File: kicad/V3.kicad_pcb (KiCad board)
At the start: 2 copper layers, 175.6 x 118.3 mm, 62 parts, among them U2 CH9329, U3 USB_C_C393939

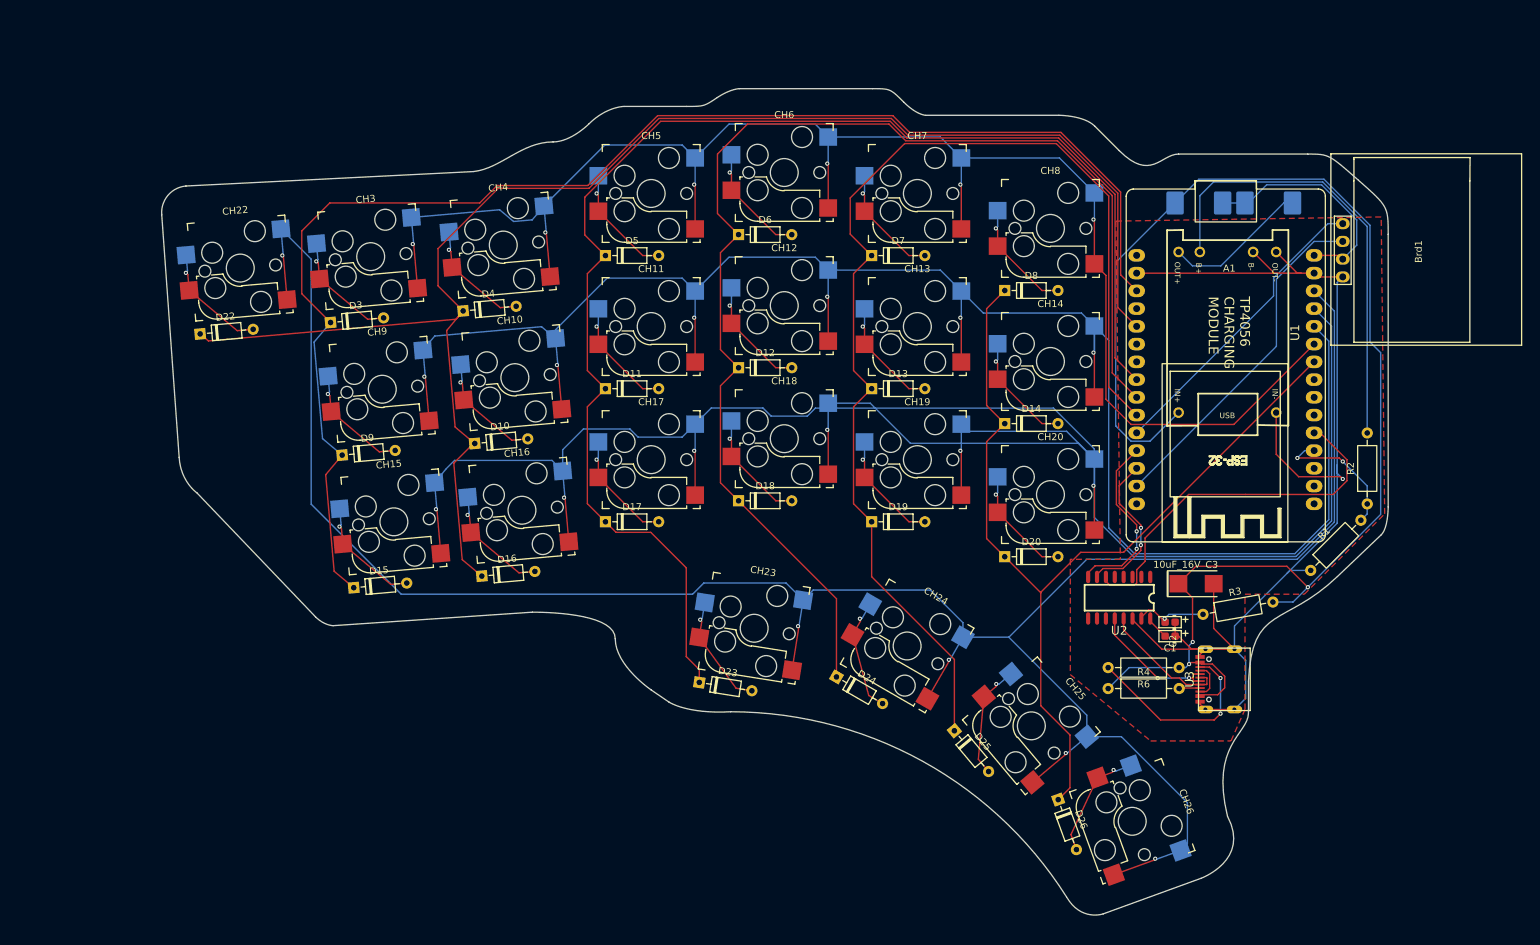
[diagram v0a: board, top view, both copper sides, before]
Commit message: switches change
switches no longer use heirarchical schematic
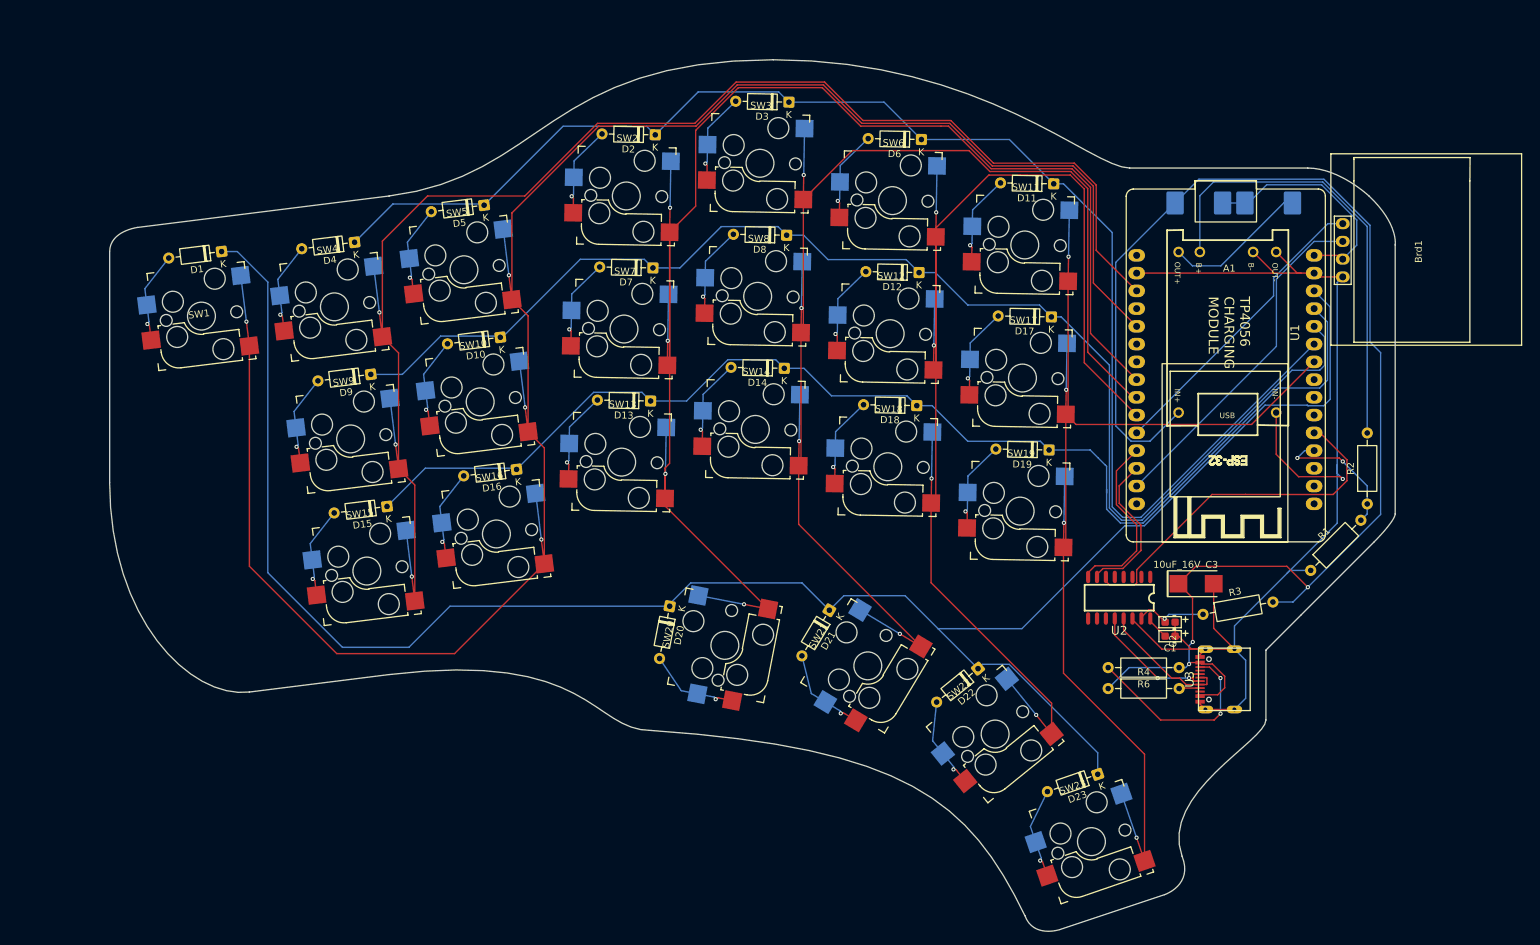
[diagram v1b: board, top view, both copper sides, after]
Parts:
- removed CH10, CH11, CH12, CH13, CH14, CH15, CH16, CH17, CH18, CH19, CH20, CH22, CH23, CH24, CH25, CH26, CH3, CH4, CH5, CH6, CH7, CH8, CH9: KS33_SW_HS, Library:Kailh_socket_MX_reversible
- removed D24, D25, D26: 1N4148, Diode_THT:D_DO-35_SOD27_P7.62mm_Horizontal
- added D1: 1N4148, Diode_THT:D_DO-35_SOD27_P7.62mm_Horizontal, F.Cu at (66.5, 64.0)
- added D2: 1N4148, Diode_THT:D_DO-35_SOD27_P7.62mm_Horizontal, F.Cu at (128.6, 47.2)
- added D21: 1N4148, Diode_THT:D_DO-35_SOD27_P7.62mm_Horizontal, F.Cu at (153.5, 115.3)
- added SW1: KS33_SW_HS, keyswitches:Kailh_socket_MX_reversible, F.Cu at (63.6, 73.2)
- added SW10: KS33_SW_HS, keyswitches:Kailh_socket_MX_reversible, F.Cu at (103.5, 85.5)
- added SW11: KS33_SW_HS, keyswitches:Kailh_socket_MX_reversible, F.Cu at (181.5, 63.0)
- added SW12: KS33_SW_HS, keyswitches:Kailh_socket_MX_reversible, F.Cu at (162.2, 75.7)
- added SW13: KS33_SW_HS, keyswitches:Kailh_socket_MX_reversible, F.Cu at (123.8, 94.1)
- added SW14: KS33_SW_HS, keyswitches:Kailh_socket_MX_reversible, F.Cu at (142.9, 89.4)
- added SW15: KS33_SW_HS, keyswitches:Kailh_socket_MX_reversible, F.Cu at (87.3, 109.7)
- added SW16: KS33_SW_HS, keyswitches:Kailh_socket_MX_reversible, F.Cu at (105.9, 104.4)
- added SW17: KS33_SW_HS, keyswitches:Kailh_socket_MX_reversible, F.Cu at (181.2, 82.1)
- added SW18: KS33_SW_HS, keyswitches:Kailh_socket_MX_reversible, F.Cu at (161.9, 94.8)
- added SW19: KS33_SW_HS, keyswitches:Kailh_socket_MX_reversible, F.Cu at (180.8, 101.1)
- added SW2: KS33_SW_HS, keyswitches:Kailh_socket_MX_reversible, F.Cu at (124.5, 56.0)
- added SW20: KS33_SW_HS, keyswitches:Kailh_socket_MX_reversible, F.Cu at (138.6, 120.3)
- added SW21: KS33_SW_HS, keyswitches:Kailh_socket_MX_reversible, F.Cu at (159.0, 123.3)
- added SW22: KS33_SW_HS, keyswitches:Kailh_socket_MX_reversible, F.Cu at (177.2, 133.0)
- added SW23: KS33_SW_HS, keyswitches:Kailh_socket_MX_reversible, F.Cu at (191.0, 148.4)
- added SW3: KS33_SW_HS, keyswitches:Kailh_socket_MX_reversible, F.Cu at (143.6, 51.3)
- added SW4: KS33_SW_HS, keyswitches:Kailh_socket_MX_reversible, F.Cu at (82.7, 71.9)
- added SW5: KS33_SW_HS, keyswitches:Kailh_socket_MX_reversible, F.Cu at (101.2, 66.6)
- added SW6: KS33_SW_HS, keyswitches:Kailh_socket_MX_reversible, F.Cu at (162.5, 56.7)
- added SW7: KS33_SW_HS, keyswitches:Kailh_socket_MX_reversible, F.Cu at (124.1, 75.0)
- added SW8: KS33_SW_HS, keyswitches:Kailh_socket_MX_reversible, F.Cu at (143.3, 70.4)
- added SW9: KS33_SW_HS, keyswitches:Kailh_socket_MX_reversible, F.Cu at (85.0, 90.8)
- moved D22 121.2 mm to (174.8, 123.6), turned to -141 degrees
- moved D3 72.8 mm to (147.7, 42.6), turned to 179 degrees
- moved D11 70.5 mm to (185.6, 54.3), turned to 179 degrees
- moved D17 70.2 mm to (185.3, 73.3), turned to 179 degrees
- moved D23 58.5 mm to (191.9, 138.8), turned to -161 degrees
- moved D20 48.5 mm to (130.7, 114.7), turned to -101 degrees
- moved D14 32.5 mm to (147.1, 80.7), turned to 179 degrees
- moved D8 32.2 mm to (147.4, 61.6), turned to 179 degrees
- moved D13 31.7 mm to (127.9, 85.3), turned to 179 degrees
- moved D7 31.4 mm to (128.3, 66.3), turned to 179 degrees
- moved D6 29.5 mm to (166.7, 47.9), turned to 179 degrees
- moved D12 29.2 mm to (166.4, 67.0), turned to 179 degrees
- moved D18 28.9 mm to (166.0, 86.0), turned to 179 degrees
- moved D19 27.4 mm to (185.0, 92.4), turned to 179 degrees
- moved D5 18.8 mm to (104.1, 57.3), turned to -173 degrees
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- renumbered D1 to DS1, D21 to DS2
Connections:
- net Net-(BT1-+) renamed /B+
- D10 pad 1: /Col2 -> /Row2
- D11 pad 1: /Col3 -> /Row1
- D12 pad 1: /Col4 -> /Row2
- D13 pad 1: /Col5 -> /Row3
- D14 pad 1: /Col6 -> /Row3
- D15 pad 1: /Col1 -> /Row3
- D16 pad 1: /Col2 -> /Row3
- D17 pad 1: /Col3 -> /Row2
- D18 pad 1: /Col4 -> /Row3
- D19 pad 1: /Col5 -> /Row3
- D20 pad 1: /Col6 -> /Row4
- D22 pad 1: /Col2 -> /Row4
- D23 pad 1: /Col3 -> /Row4
- D3 pad 1: /Col1 -> /Row1
- D4 pad 1: /Col2 -> /Row1
- D5 pad 1: /Col3 -> /Row1
- D6 pad 1: /Col4 -> /Row1
- D7 pad 1: /Col5 -> /Row2
- D8 pad 1: /Col6 -> /Row2
- D9 pad 1: /Col1 -> /Row2
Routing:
- net /Row3: track 310.1 -> 177.8 mm, vias 6 -> 0
- net /Row2: track 267.8 -> 191.2 mm, vias 6 -> 0
- net /Col2: track 221.6 -> 296.5 mm, vias 0 -> 4
- net /Row4: track 336.2 -> 278.9 mm, vias 5 -> 0
- net /Col5: track 163.1 -> 200.3 mm, vias 0 -> 4
- net /Col3: track 196.0 -> 231.5 mm, vias 0 -> 4
- net /Col6: track 134.6 -> 168.5 mm, vias 0 -> 4
- net /Row1: track 227.6 -> 205.9 mm, vias 6 -> 0
- net /Col1: track 200.9 -> 219.1 mm, vias 0 -> 3
- net Net-(D25-A): track 16.6 -> 0.00 mm, vias 1 -> 0
- net Net-(D24-A): track 16.6 -> 0.00 mm, vias 1 -> 0
- net Net-(D26-A): track 16.6 -> 0.00 mm, vias 1 -> 0
- net Net-(D21-A): track 0.00 -> 13.2 mm, vias 0 -> 1
- net Net-(D2-A): track 0.00 -> 13.2 mm, vias 0 -> 1
- net Net-(D1-A): track 0.00 -> 13.2 mm, vias 0 -> 1
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- removed copper zone on F.Cu, net Earth
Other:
- board size 175.6 x 118.3 mm -> 184 x 124.7 mm

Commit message: outline changes
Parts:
- moved R2 15.5 mm to (229.5, 84.6)
- moved R1 13.9 mm to (229.5, 97.6), turned to 90 degrees
- moved R4 12.5 mm to (205.9, 125.8)
- moved U3 12.5 mm to (219.8, 124.5)
- moved C1 12.5 mm to (214.8, 118.3)
- moved C2 12.5 mm to (214.8, 116.3)
- moved C3 12.5 mm to (218.5, 110.8)
- moved R3 12.5 mm to (219.5, 115.2), turned to 0 degrees
- moved R6 12.5 mm to (216.1, 122.8)
- moved U2 12.5 mm to (207.5, 112.8)
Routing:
- net +5V: track 200.2 -> 133.0 mm, vias 3 -> 5
- net /B+: track 65.0 -> 44.0 mm, vias 0 -> 1
- net Earth: track 172.5 -> 154.1 mm
- net /USB_rst: track 52.0 -> 38.6 mm
- net /ADC_batt: track 19.8 -> 15.4 mm, vias 2 -> 0
- net /RX: track 25.6 -> 22.1 mm
- net /Col2: track 296.5 -> 294.0 mm
- net /TX: track 22.1 -> 19.7 mm
- net /Row4: track 278.9 -> 276.7 mm
- net /~3v3: track 33.1 -> 35.1 mm
- net /Row3: track 177.8 -> 177.3 mm
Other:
- board size 184 x 124.7 mm -> 180.5 x 123.2 mm

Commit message: graphic change
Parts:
- moved REF** 140.2 mm to (200.6, 128.2)
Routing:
- net Earth: track 154.1 -> 170.2 mm
- net +5V: track 133.0 -> 128.5 mm
- net /USB_rst: track 38.6 -> 38.0 mm

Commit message: power
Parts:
- removed Brd1: SSD1306, Library:SSD1306
- removed REF**: Sig, Library:Sig
- added U4: SSD1306-128X64-OLED-0.96, Library:SSD1306, F.Cu at (253.1, 77.5)
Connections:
- A1 pad 1: unconnected-(A1-3.3V-Pad1) -> +3V3
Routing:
- net +3V3: track 0.00 -> 36.5 mm
- net /~3v3: track 35.1 -> 17.4 mm, vias 0 -> 2
- net /SCL: track 49.6 -> 51.7 mm
- net Earth: track 170.2 -> 171.7 mm, vias 1 -> 2
- net /SDA: track 43.4 -> 44.2 mm

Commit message: working version
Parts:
- removed A1: ESP32_DevKit_V1_DOIT_30GPIOs, PCM_SL_Development_Boards:DOIT_ESP32_DEVKIT_30Pins
- removed C1, C2: 0.1uF_0603_16V, PCM_Capacitor_Tantalum_SMD_Handsoldering_AKL:CP_EIA-1608-08_AVX-J
- removed C3: 10uF_16V, PCM_4ms_Capacitor:CP_Tantalum_EIA-6032-28_Kemet-C
- removed D23: 1N4148, Diode_THT:D_DO-35_SOD27_P7.62mm_Horizontal
- removed DS1, DS2: SS34, PCM_Diode_SMD_AKL:D_SMC
- removed R1: 270k, Resistor_THT:R_Axial_DIN0207_L6.3mm_D2.5mm_P10.16mm_Horizontal
- removed R2: 100k, Resistor_THT:R_Axial_DIN0207_L6.3mm_D2.5mm_P10.16mm_Horizontal
- removed R3: 1R, Resistor_THT:R_Axial_DIN0207_L6.3mm_D2.5mm_P10.16mm_Horizontal
- removed R4, R6: 5.1k, Resistor_THT:R_Axial_DIN0207_L6.3mm_D2.5mm_P10.16mm_Horizontal
- removed U2: CH9329, Library:CH9329
- removed U3: USB_C_C393939, Library:USBC_C393939
- D1, D10, D11, D12, D13, D14, D15, D16, D17, D18, D19, D2, D20, D21, D22, D3, D4, D5, D6, D7, D8, D9: footprint Diode_THT:D_DO-35_SOD27_P7.62mm_Horizontal -> PCM_Diode_THT_AKL:D_DO-35_SOD27_P7.62mm_Horizontal
- SW1, SW10, SW11, SW12, SW13, SW14, SW15, SW16, SW17, SW18, SW19, SW2, SW20, SW21, SW22, SW3, SW4, SW5, SW6, SW7, SW8, SW9: footprint keyswitches:Kailh_socket_MX_reversible -> keyswitches:Kailh_socket_PG1350_reversible
- SW23: value KS33_SW_HS -> Slide_Switch_SPDT_P3mm_10x5x10mm; footprint keyswitches:Kailh_socket_MX_reversible -> PCM_SL_Devices:Slide_Switch_SPDT_P3mm_10x5x10mm
- U1: value ~ -> SuperMini nRF52840; footprint Library:HAYATEC TP4056 LIPO CHARGING MODULE -> PCM_marbastlib-xp-promicroish:SuperMini_nRF52840_AH_USBup
- moved D11 114.0 mm to (76.9, 88.5), turned to -172 degrees
- moved D17 111.1 mm to (79.5, 107.4), turned to -172 degrees
- moved SW11 109.7 mm to (73.2, 80.4), turned to 8 degrees
- moved D18 108.3 mm to (61.1, 113.0), turned to -172 degrees
- moved SW17 106.8 mm to (75.8, 99.3), turned to 8 degrees
- moved SW18 105.0 mm to (57.4, 104.9), turned to 8 degrees
- moved U4 98.7 mm to (158.3, 104.9), turned to 0 degrees
- moved D7 73.0 mm to (55.8, 75.3), turned to -172 degrees
- moved SW7 72.5 mm to (52.1, 67.2), turned to 8 degrees
- moved D13 70.0 mm to (58.4, 94.1), turned to -172 degrees
- moved SW4 69.7 mm to (150.5, 56.0), turned to 0 degrees
- moved SW13 69.5 mm to (54.7, 86.1), turned to 8 degrees
- moved D19 68.6 mm to (121.7, 118.8), turned to 170 degrees
- moved D4 67.6 mm to (153.1, 64.5), turned to 180 degrees
- moved SW19 60.9 mm to (120.6, 110.0), turned to -10 degrees
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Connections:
- D1 pad 1: /Row4 -> /Row1
- D11 pad 1: /Row1 -> /Row2
- D12 pad 1: /Row2 -> /Row3
- D13 pad 1: /Row3 -> /Row2
- D17 pad 1: /Row2 -> /Row3
- D19 pad 1: /Row3 -> /Row4
- D6 pad 1: /Row1 -> /Row2
- D7 pad 1: /Row2 -> /Row1
- SW1 pad 1: /Col2 -> /Col4
- SW10 pad 1: /Col2 -> /Col6
- SW11 pad 1: /Col6 -> /Col2
- SW12 pad 1: /Col5 -> /Col4
- SW13 pad 1: /Col3 -> /Col1
- SW14 pad 1: /Col4 -> /Col5
- SW15 pad 1: /Col1 -> /Col3
- SW16 pad 1: /Col2 -> /Col6
- SW17 pad 1: /Col6 -> /Col2
- SW18 pad 1: /Col5 -> /Col1
- SW19 pad 1: /Col6 -> /Col3
- SW2 pad 1: /Col3 -> /Col5
- SW20 pad 1: /Col3 -> /Col4
- SW21 pad 1: /Col4 -> /Col5
- SW22 pad 1: /Col5 -> /Col6
- SW23 pad 1: /Col6 -> Net-(BT1-+)
- SW23 pad 2: Net-(D23-A) -> unconnected-(SW23-Pad2)
- SW3 pad 1: /Col4 -> /Col3
- SW4 pad 1: /Col1 -> /Col6
- SW6 pad 1: /Col5 -> /Col4
- SW7 pad 1: /Col3 -> /Col1
- SW8 pad 1: /Col4 -> /Col5
- SW9 pad 1: /Col1 -> /Col3
- U1 pad 1: Earth -> unconnected-(U1-P0.06-Pad1)
- U1 pad 2: +5V -> unconnected-(U1-P0.08-Pad2)
- U1 pad 5: /B+ -> /SDA
- U1 pad 6: Net-(DS2-A) -> /SCL
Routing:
- net /Row4: track 276.7 -> 145.1 mm
- net +5V: track 128.5 -> 0.00 mm, vias 5 -> 0
- net /Col2: track 294.0 -> 185.1 mm, vias 4 -> 2
- net Earth: track 171.7 -> 70.4 mm, vias 2 -> 0
- net /Row1: track 205.9 -> 142.2 mm
- net /Row2: track 191.2 -> 147.3 mm
- net /USB_rst: track 38.0 -> 0.00 mm
- net /B+: track 44.0 -> 73.1 mm, vias 1 -> 0
- net /HID connector/CC2: track 28.2 -> 0.00 mm, vias 2 -> 0
- net /Col3: track 231.5 -> 206.5 mm
- net /RX: track 22.1 -> 0.00 mm
- net /SCL: track 51.7 -> 30.1 mm
- net Net-(DS2-A): track 20.9 -> 0.00 mm
- net /TX: track 19.7 -> 0.00 mm
- net /Col4: track 191.1 -> 210.2 mm, vias 4 -> 5
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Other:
- board size 180.5 x 123.2 mm -> 150.9 x 130.2 mm
